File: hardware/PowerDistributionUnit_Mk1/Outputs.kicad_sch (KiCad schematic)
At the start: 23 parts, among them U25 NL17SZS11DFT2G-Q

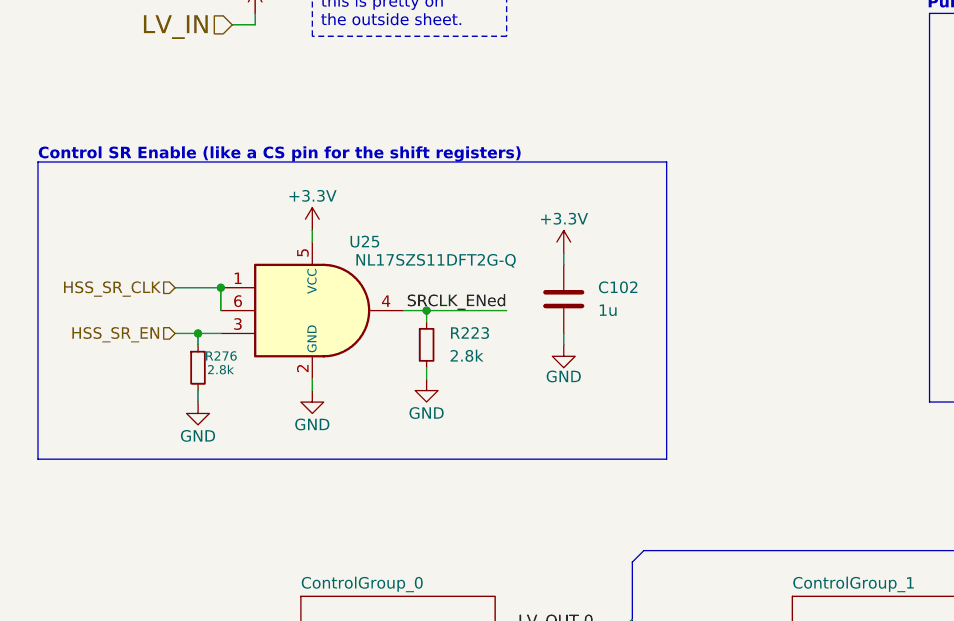
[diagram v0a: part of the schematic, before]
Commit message: add SRCLK_ENed connection to logic analyzer connector
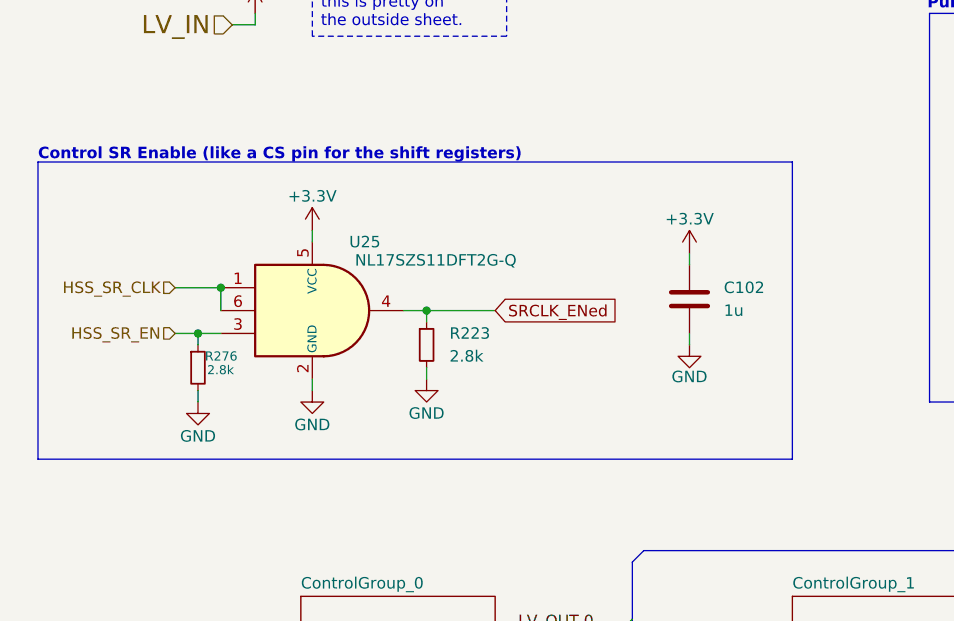
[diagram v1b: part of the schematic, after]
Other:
- moved on the sheet: C102
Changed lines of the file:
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@@
 	(rectangle
 		(start 20.32 45.72)
-		(end 90.17 78.74)
+		(end 104.14 78.74)
 		(stroke
 			(width 0)
@@
 	(wire
 		(pts
-			(xy 78.74 64.77) (xy 78.74 66.04)
+			(xy 92.71 64.77) (xy 92.71 66.04)
 		)
 		(stroke
@@
 	(wire
 		(pts
-			(xy 78.74 55.88) (xy 78.74 57.15)
+			(xy 92.71 55.88) (xy 92.71 57.15)
 		)
 		(stroke
@@
 	(wire
 		(pts
-			(xy 63.5 62.23) (xy 72.39 62.23)
+			(xy 63.5 62.23) (xy 71.12 62.23)
 		)
 		(stroke
@@
 		)
 	)
-	(label "SRCLK_ENed"
-		(at 72.39 62.23 180)
-		(effects
-			(font
-				(size 1.27 1.27)
-			)
-			(justify right bottom)
-		)
-	)
 	(label "~{ST}.1"
 		(at 74.93 130.81 0)
@@
 		)
 	)
+	(global_label "SRCLK_ENed"
+		(shape input)
+		(at 71.12 62.23 0)
+		(fields_autoplaced yes)
+		(effects
+			(font
+				(size 1.27 1.27)
+			)
+			(justify left)
+		)
+		(property "Intersheetrefs" "${INTERSHEET_REFS}"
+			(at 85.8375 62.23 0)
+			(effects
+				(font
+					(size 1.27 1.27)
+				)
+				(justify left)
+				(hide yes)
+			)
+		)
+	)
 	(hierarchical_label "SNS.[0..15]"
 		(shape output)
@@
 	(symbol
 		(lib_id "power:+3.3V")
-		(at 78.74 55.88 0)
+		(at 92.71 55.88 0)
 		(unit 1)
 		(exclude_from_sim no)
@@
 		(dnp no)
 		(property "Reference" "#PWR016"
-			(at 78.74 59.69 0)
+			(at 92.71 59.69 0)
 			(effects
 				(font
@@
 		)
 		(property "Value" "+3.3V"
-			(at 78.74 52.07 0)
+			(at 92.71 52.07 0)
 			(effects
 				(font
@@
 		)
 		(property "Footprint" ""
-			(at 78.74 55.88 0)
+			(at 92.71 55.88 0)
 			(effects
 				(font
@@
 		)
 		(property "Datasheet" ""
-			(at 78.74 55.88 0)
+			(at 92.71 55.88 0)
 			(effects
 				(font
@@
 		)
 		(property "Description" "Power symbol creates a global label with name \"+3.3V\""
-			(at 78.74 55.88 0)
+			(at 92.71 55.88 0)
 			(effects
 				(font
@@
 	(symbol
 		(lib_id "PowerDistributionUnitCapacitorLib:1u")
-		(at 78.74 60.96 0)
+		(at 92.71 60.96 0)
 		(unit 1)
 		(exclude_from_sim no)
@@
 		(fields_autoplaced yes)
 		(property "Reference" "C102"
-			(at 82.55 59.6899 0)
+			(at 96.52 59.6899 0)
 			(effects
 				(font
@@
 		)
 		(property "Value" "1u"
-			(at 82.55 62.2299 0)
+			(at 96.52 62.2299 0)
 			(effects
 				(font
@@
 		)
 		(property "Footprint" "Capacitor_SMD:C_0603_1608Metric"
-			(at 79.7052 64.77 0)
+			(at 93.6752 64.77 0)
 			(effects
 				(font
@@
 		)
 		(property "Datasheet" "kicad-embed://MLR01_e.pdf"
-			(at 78.74 60.96 0)
+			(at 92.71 60.96 0)
 			(effects
 				(font
@@
 		)
 		(property "Description" "Unpolarized capacitor"
-			(at 78.74 60.96 0)
+			(at 92.71 60.96 0)
 			(effects
 				(font
@@
 		)
 		(property "P/N" "MLASU168SB5105KTNA01"
-			(at 78.74 60.96 0)
+			(at 92.71 60.96 0)
 			(effects
 				(font
@@
 		)
 		(property "Mouser P/N" "963-MLASU168SB5105KT"
-			(at 78.74 60.96 0)
+			(at 92.71 60.96 0)
 			(effects
 				(font
@@
 		)
 		(property "Digikey P/N" ""
-			(at 78.74 60.96 0)
+			(at 92.71 60.96 0)
 			(effects
 				(font
@@
 	(symbol
 		(lib_id "power:GND")
-		(at 78.74 66.04 0)
+		(at 92.71 66.04 0)
 		(unit 1)
 		(exclude_from_sim no)
@@
 		(dnp no)
 		(property "Reference" "#PWR018"
-			(at 78.74 72.39 0)
+			(at 92.71 72.39 0)
 			(effects
 				(font
@@
 		)
 		(property "Value" "GND"
-			(at 78.74 69.596 0)
+			(at 92.71 69.596 0)
 			(effects
 				(font
@@
 		)
 		(property "Footprint" ""
-			(at 78.74 66.04 0)
+			(at 92.71 66.04 0)
 			(effects
 				(font
@@
 		)
 		(property "Datasheet" ""
-			(at 78.74 66.04 0)
+			(at 92.71 66.04 0)
 			(effects
 				(font
@@
 		)
 		(property "Description" "Power symbol creates a global label with name \"GND\" , ground"
-			(at 78.74 66.04 0)
+			(at 92.71 66.04 0)
 			(effects
 				(font

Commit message: update all symbols with LCSC P/N
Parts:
- C102: LCSC P/N (none) -> C15849
- R10, R11, R12, R223, R227, R235, R239, R276, R7, R8, R9: LCSC P/N (none) -> C844548
- U25: LCSC P/N (none) -> C23078196
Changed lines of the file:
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@@
+			)
+		)
+		(property "LCSC P/N" "C844548"
+			(at 185.42 54.61 0)
+			(effects
+				(font
+					(size 1.27 1.27)
+				)
+				(hide yes)
 			)
 		)
@@
 		)
 		(property "Digikey P/N" "541-2.80KHCT-ND"
+			(at 185.42 45.72 0)
+			(effects
+				(font
+					(size 1.27 1.27)
+				)
+				(hide yes)
+			)
+		)
+		(property "LCSC P/N" "C844548"
 			(at 185.42 45.72 0)
 			(effects
@@
 			)
 		)
+		(property "LCSC P/N" "C844548"
+			(at 199.39 45.72 0)
+			(effects
+				(font
+					(size 1.27 1.27)
+				)
+				(hide yes)
+			)
+		)
 		(pin "2"
 		)
@@
 			)
 		)
+		(property "LCSC P/N" "C844548"
+			(at 165.1 41.91 0)
+			(effects
+				(font
+					(size 1.27 1.27)
+				)
+				(hide yes)
+			)
+		)
 		(pin "2"
 		)
@@
 		)
 		(property "Digikey P/N" "541-2.80KHCT-ND"
+			(at 63.5 66.04 0)
+			(effects
+				(font
+					(size 1.27 1.27)
+				)
+				(hide yes)
+			)
+		)
+		(property "LCSC P/N" "C844548"
 			(at 63.5 66.04 0)
 			(effects
@@
 			)
 		)
+		(property "LCSC P/N" "C844548"
+			(at 199.39 54.61 0)
+			(effects
+				(font
+					(size 1.27 1.27)
+				)
+				(hide yes)
+			)
+		)
 		(pin "2"
 		)
@@
 			)
 		)
+		(property "LCSC P/N" "C844548"
+			(at 165.1 52.07 0)
+			(effects
+				(font
+					(size 1.27 1.27)
+				)
+				(hide yes)
+			)
+		)
 		(pin "2"
 		)
@@
 			)
 		)
+		(property "LCSC P/N" "C844548"
+			(at 38.1 68.58 0)
+			(effects
+				(font
+					(size 1.27 1.27)
+				)
+				(hide yes)
+			)
+		)
 		(pin "2"
 		)
@@
 		)
 		(property "Digikey P/N" "488-NL17SZS11DFT2G-QCT-ND"
+			(at 52.07 62.23 0)
+			(effects
+				(font
+					(size 1.27 1.27)
+				)
+				(hide yes)
+			)
+		)
+		(property "LCSC P/N" "C23078196"
 			(at 52.07 62.23 0)
 			(effects
@@
 			)
 		)
+		(property "LCSC P/N" "C15849"
+			(at 92.71 60.96 0)
+			(effects
+				(font
+					(size 1.27 1.27)
+				)
+				(hide yes)
+			)
+		)
 		(pin "1"
 		)
@@
 		)
 		(property "Digikey P/N" "541-2.80KHCT-ND"
+			(at 138.43 48.26 0)
+			(effects
+				(font
+					(size 1.27 1.27)
+				)
+				(hide yes)
+			)
+		)
+		(property "LCSC P/N" "C844548"
 			(at 138.43 48.26 0)
 			(effects
@@
 			)
 		)
+		(property "LCSC P/N" "C844548"
+			(at 212.09 45.72 0)
+			(effects
+				(font
+					(size 1.27 1.27)
+				)
+				(hide yes)
+			)
+		)
 		(pin "2"
 		)
@@
 			(at 212.09 54.61 0)
 			(effects
+				(font
+					(size 1.27 1.27)
+				)
+				(hide yes)
+			)
+		)
+		(property "LCSC P/N" "C844548"
+			(at 212.09 54.61 0)
+			(effects

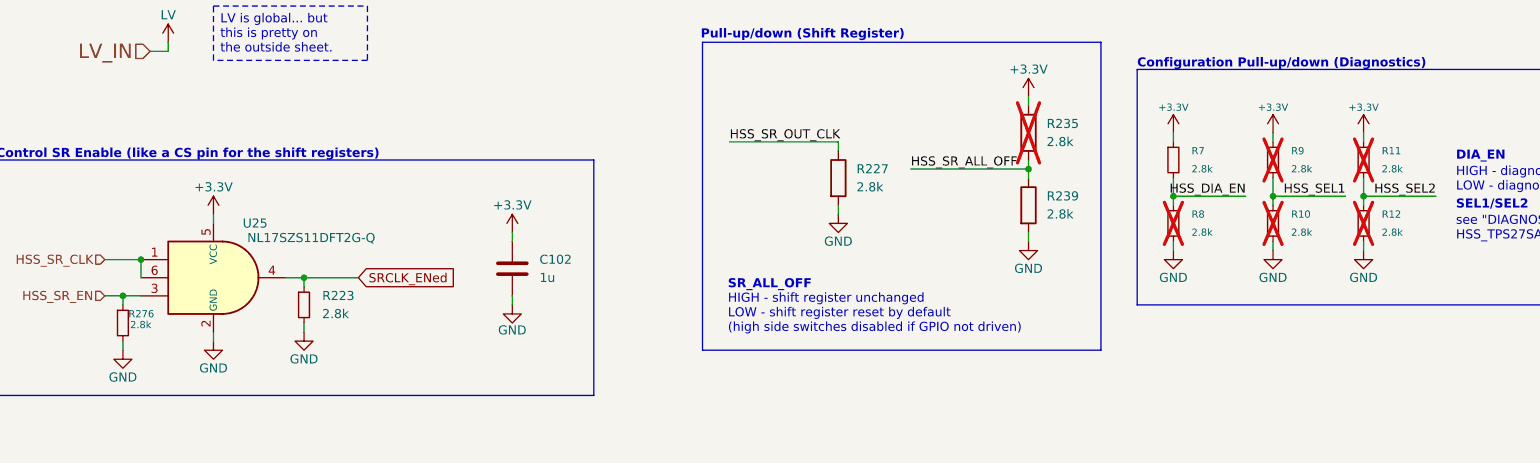
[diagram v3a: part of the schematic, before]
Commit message: change lv sense rdiv values to avoid extended components, update all pull-ups/-downs using 2.8k
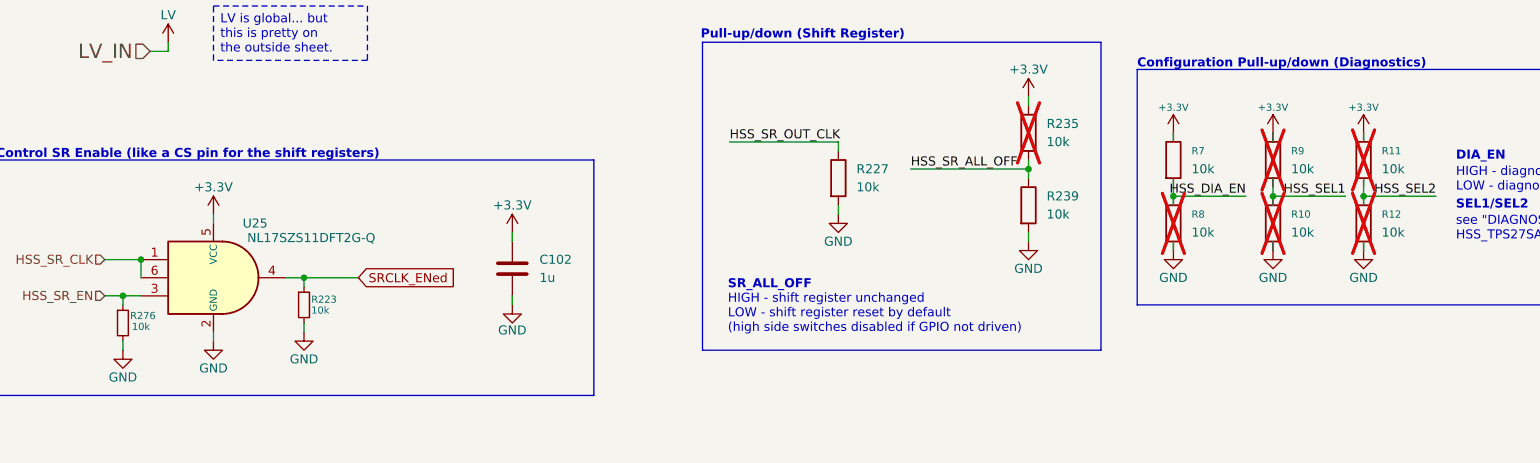
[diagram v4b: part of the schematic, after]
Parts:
- R10, R11, R12, R7, R8, R9: value 2.8k -> 10k; symbol PowerDistributionUnitResistorLib:2.8k_Small -> PowerDistributionUnitResistorLib:10k; LCSC P/N C844548 -> C25804; Mouser P/N 71-CRCW0603-2.8K-E3 -> 71-CRCW060310K0FKEI; P/N CRCW06032K80FKEA -> CRCW060310K0FKEI
- R223, R276: value 2.8k -> 10k; symbol PowerDistributionUnitResistorLib:2.8k_Small -> PowerDistributionUnitResistorLib:10k_Small; LCSC P/N C844548 -> C25804; Mouser P/N 71-CRCW0603-2.8K-E3 -> 71-CRCW060310K0FKEI; P/N CRCW06032K80FKEA -> CRCW060310K0FKEI
- R227, R235, R239: value 2.8k -> 10k; symbol PowerDistributionUnitResistorLib:2.8k -> PowerDistributionUnitResistorLib:10k; LCSC P/N C844548 -> C25804; Mouser P/N 71-CRCW0603-2.8K-E3 -> 71-CRCW060310K0FKEI; P/N CRCW06032K80FKEA -> CRCW060310K0FKEI
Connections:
- net HSS_DIA_EN: no longer R7.2
- net HSS_SEL1: no longer R9.2
- net HSS_SEL2: no longer R11.2

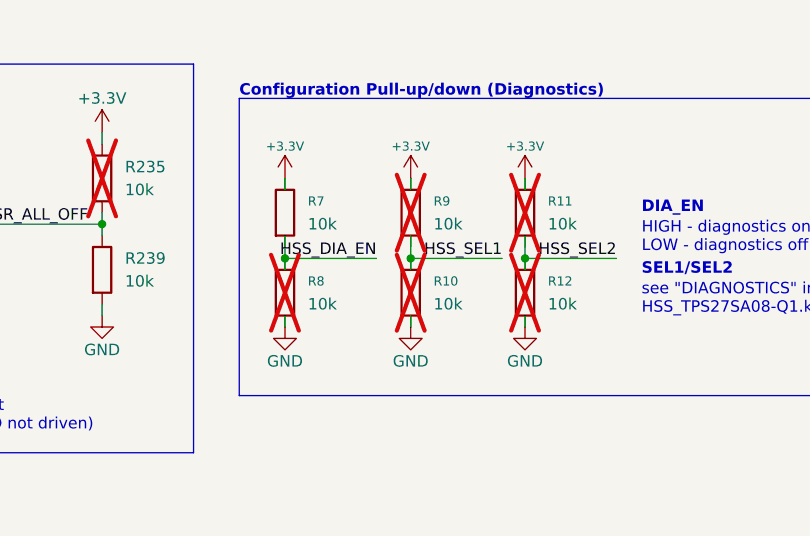
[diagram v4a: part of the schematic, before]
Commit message: fix shorted nets error from wrong size res symbol from resistor change
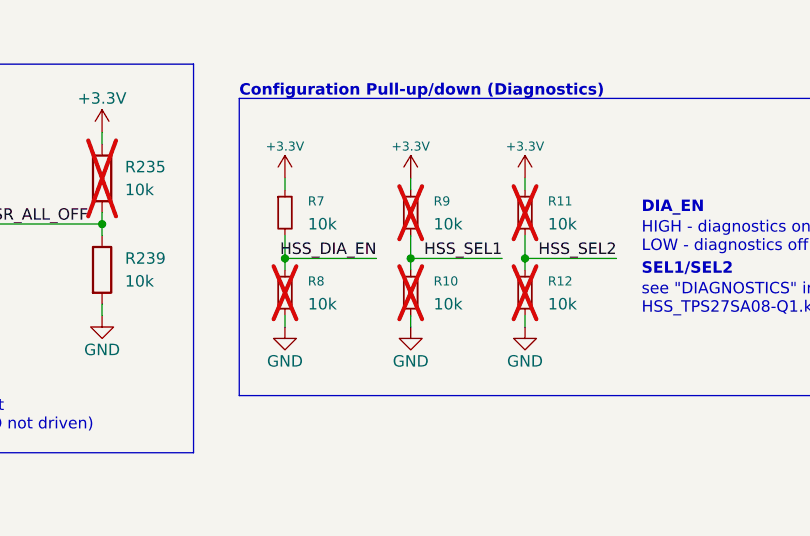
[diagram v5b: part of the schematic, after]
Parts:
- R10, R11, R12, R7, R8, R9: symbol PowerDistributionUnitResistorLib:10k -> PowerDistributionUnitResistorLib:10k_Small
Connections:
- net HSS_DIA_EN: now also R7.2
- net HSS_SEL1: now also R9.2
- net HSS_SEL2: now also R11.2
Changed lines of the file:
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@@
 	)
 	(symbol
-		(lib_id "PowerDistributionUnitResistorLib:10k")
+		(lib_id "PowerDistributionUnitResistorLib:10k_Small")
 		(at 185.42 54.61 0)
 		(unit 1)
@@
 			)
 		)
-		(property "Description" "Resistor"
+		(property "Description" "Resistor, small symbol"
 			(at 185.42 54.61 0)
 			(effects
@@
 	)
 	(symbol
-		(lib_id "PowerDistributionUnitResistorLib:10k")
+		(lib_id "PowerDistributionUnitResistorLib:10k_Small")
 		(at 185.42 45.72 0)
 		(unit 1)
@@
 			)
 		)
-		(property "Description" "Resistor"
+		(property "Description" "Resistor, small symbol"
 			(at 185.42 45.72 0)
 			(effects
@@
 	)
 	(symbol
-		(lib_id "PowerDistributionUnitResistorLib:10k")
+		(lib_id "PowerDistributionUnitResistorLib:10k_Small")
 		(at 199.39 45.72 0)
 		(unit 1)
@@
 			)
 		)
-		(property "Description" "Resistor"
+		(property "Description" "Resistor, small symbol"
 			(at 199.39 45.72 0)
 			(effects
@@
 	)
 	(symbol
-		(lib_id "PowerDistributionUnitResistorLib:10k")
+		(lib_id "PowerDistributionUnitResistorLib:10k_Small")
 		(at 199.39 54.61 0)
 		(unit 1)
@@
 			)
 		)
-		(property "Description" "Resistor"
+		(property "Description" "Resistor, small symbol"
 			(at 199.39 54.61 0)
 			(effects
@@
 	)
 	(symbol
-		(lib_id "PowerDistributionUnitResistorLib:10k")
+		(lib_id "PowerDistributionUnitResistorLib:10k_Small")
 		(at 212.09 45.72 0)
 		(unit 1)
@@
 			)
 		)
-		(property "Description" "Resistor"
+		(property "Description" "Resistor, small symbol"
 			(at 212.09 45.72 0)
 			(effects
@@
 	)
 	(symbol
-		(lib_id "PowerDistributionUnitResistorLib:10k")
+		(lib_id "PowerDistributionUnitResistorLib:10k_Small")
 		(at 212.09 54.61 0)
 		(unit 1)
@@
 			)
 		)
-		(property "Description" "Resistor"
+		(property "Description" "Resistor, small symbol"
 			(at 212.09 54.61 0)
 			(effects
